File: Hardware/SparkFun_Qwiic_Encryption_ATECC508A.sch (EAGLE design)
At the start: 22 parts, among them J1 QWIIC, J2 QWIIC, J3 PTH, U1 ATECC508A

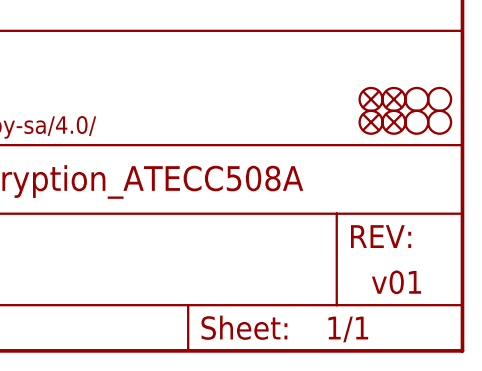
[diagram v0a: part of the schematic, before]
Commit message: Changed silk to correct product name
Also updated sch and board to "v10".
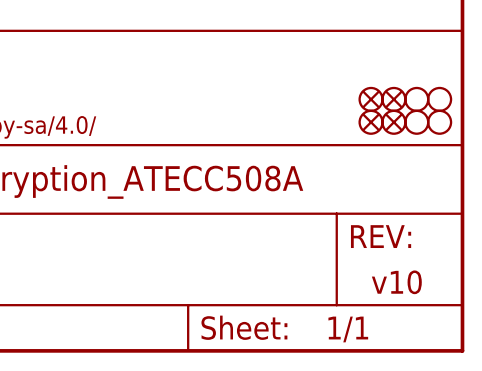
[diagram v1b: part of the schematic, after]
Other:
- note added: "v10"
- note removed: "v01"
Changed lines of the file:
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@@
 to 4.7k pull-up
 resistors.</text>
-<text x="238.76" y="7.62" size="2.54" layer="94" font="vector" align="center-left">v01</text>
+<text x="238.76" y="7.62" size="2.54" layer="94" font="vector" align="center-left">v10</text>
 <text x="165.862" y="11.176" size="2.54" layer="94" font="vector">Pete Lewis</text>
 <wire x1="248.92" y1="91.44" x2="0" y2="91.44" width="0.2032" layer="97" style="shortdash"/>

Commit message: rename and adjusted silk for protos
version to v01
added silk to bplace with name
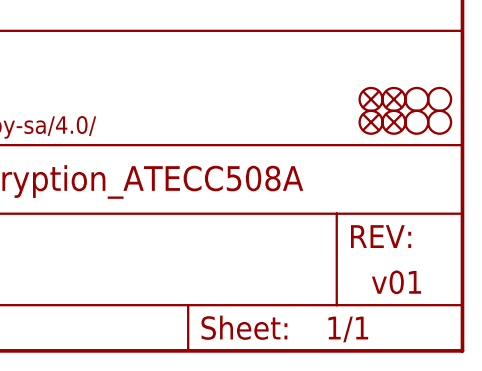
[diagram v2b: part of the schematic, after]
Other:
- note added: "v01"
- note removed: "v10"
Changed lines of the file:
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@@
 to 4.7k pull-up
 resistors.</text>
-<text x="238.76" y="7.62" size="2.54" layer="94" font="vector" align="center-left">v10</text>
+<text x="238.76" y="7.62" size="2.54" layer="94" font="vector" align="center-left">v01</text>
 <text x="165.862" y="11.176" size="2.54" layer="94" font="vector">Pete Lewis</text>
 <wire x1="248.92" y1="91.44" x2="0" y2="91.44" width="0.2032" layer="97" style="shortdash"/>
